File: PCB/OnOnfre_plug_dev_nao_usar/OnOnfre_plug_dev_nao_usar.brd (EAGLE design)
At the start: 44.4 x 47.7 mm, 41 parts, among them IC4 HLW8012, J7 8p, Q3 2N7002, Q4 2N7002, U2 esp12

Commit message: Labels Fix
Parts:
- removed R5: VARISTORS07K230, varistor:S07K230
- moved R31 113.5 mm to (22.1, 38.4), turned to 180 degrees
- moved R45 111.2 mm to (25.4, 38.4)
- moved R47 110.2 mm to (28.4, 37.8), turned to 270 degrees
- moved R48 110.1 mm to (31.0, 37.8), turned to 90 degrees
- moved R32 109.5 mm to (30.5, 33.0), turned to 180 degrees
- moved R46 108.5 mm to (25.4, 36.1), turned to 180 degrees
- moved R49 100.5 mm to (42.7, 27.2), turned to 180 degrees
- moved R55 98.4 mm to (17.3, 21.3), turned to 180 degrees
- moved R54 97.2 mm to (17.3, 19.6), turned to 180 degrees
- moved R53 96.3 mm to (17.3, 17.8), turned to 180 degrees
- moved R50 96.0 mm to (17.3, 23.4)
- moved R52 90.1 mm to (17.3, 16.0), turned to 180 degrees
- moved C44 89.8 mm to (6.10, 22.4), turned to 270 degrees
- moved C42 89.5 mm to (3.05, 22.4), turned to 270 degrees
- moved R43 88.4 mm to (5.84, 16.5)
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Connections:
- net LINE_IN: now also U$2.P$2; no longer R5.1, U$2.P$1
- net NEUTRAL_IN: now also U$2.P$1; no longer R5.2, U$2.P$2
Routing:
- net 5V: track 45.7 -> 0.00 mm, vias 1 -> 0
- net NEUTRAL_IN: track 50.8 -> 17.2 mm
- net GND: track 81.8 -> 63.9 mm, vias 3 -> 0
- net GPIO04: track 13.9 -> 0.00 mm
- net NC: track 9.81 -> 0.00 mm
- net LINE_IN: track 7.28 -> 13.4 mm
- net NO: track 4.80 -> 0.00 mm
- net GPIO05: track 6.68 -> 3.64 mm
- net N$6: track 0.00 -> 2.26 mm
- net V2P: track 0.00 -> 2.03 mm
- net N$8: track 0.00 -> 1.78 mm
- net N$16: track 0.00 -> 1.78 mm
- net N$15: track 0.00 -> 1.78 mm
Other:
- board size 44.4 x 47.7 mm -> 44.8 x 47.8 mm
- board text removed: "230V"
- board text removed: "2A MAX"
- board text removed: "2ADSS"
- board text removed: "BH-OnOfre"
- board text removed: "DANGER HIGH VOLTAGE"
- board text removed: "rev3.4"

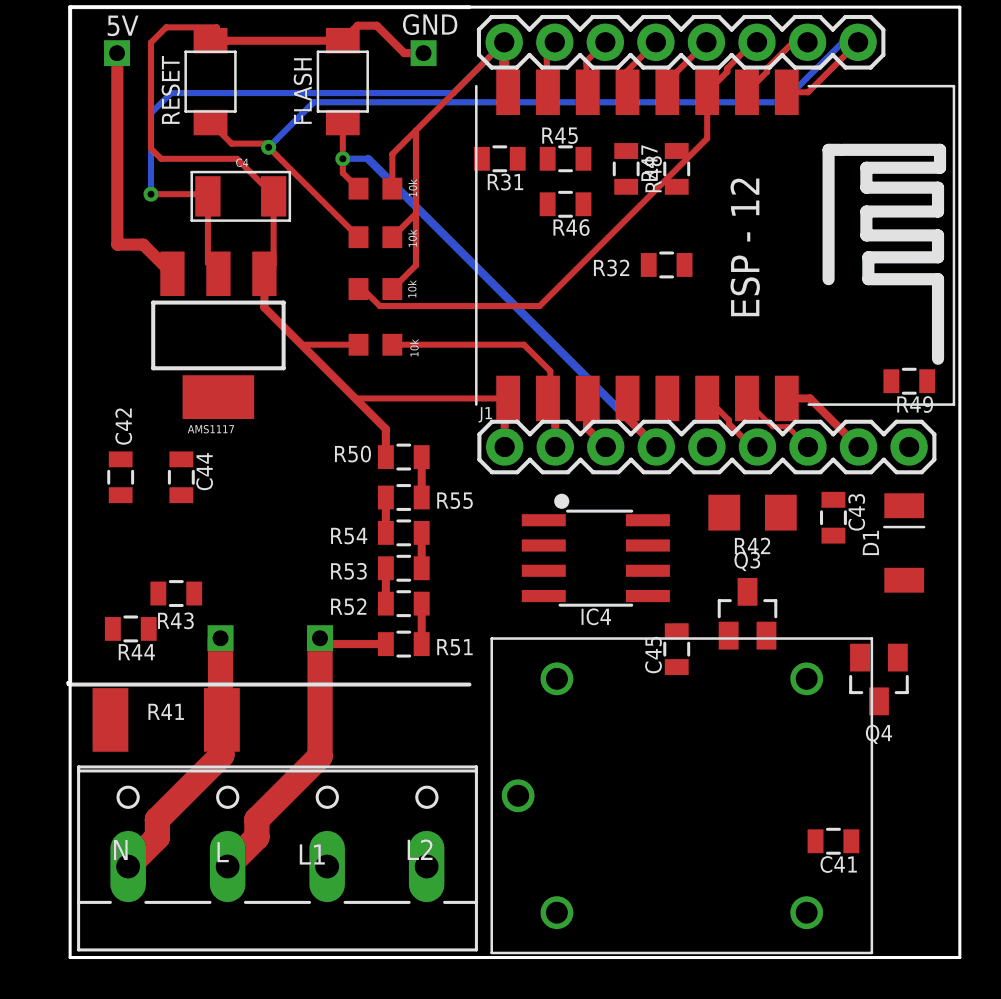
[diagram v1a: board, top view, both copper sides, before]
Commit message: remoção do OTA Arduino e adição de OTA via Web
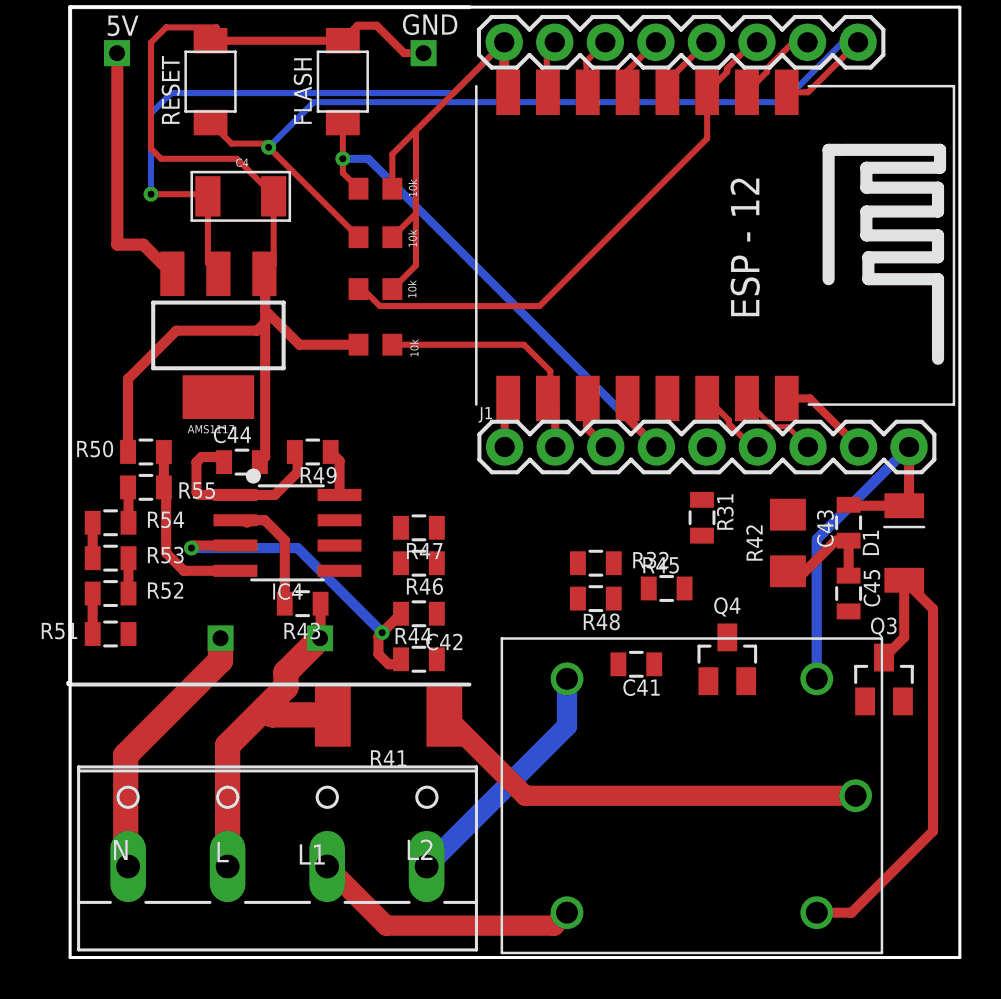
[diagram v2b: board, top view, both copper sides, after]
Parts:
- moved R49 30.2 mm to (12.7, 23.6)
- moved R45 22.2 mm to (30.5, 16.8)
- moved R48 22.0 mm to (26.9, 16.3), turned to 180 degrees
- moved R47 20.8 mm to (18.0, 19.8), turned to 180 degrees
- moved R31 20.7 mm to (32.3, 20.3), turned to 270 degrees
- moved R46 19.5 mm to (18.0, 18.0)
- moved C42 16.5 mm to (18.0, 15.5), turned to 180 degrees
- moved IC4 15.5 mm to (9.65, 21.8)
- moved R32 15.4 mm to (26.9, 18.0), turned to 0 degrees
- moved R51 14.7 mm to (2.54, 14.5), turned to 0 degrees
- moved R52 14.7 mm to (2.54, 16.5), turned to 0 degrees
- moved R53 14.7 mm to (2.54, 18.3), turned to 0 degrees
- moved R54 14.7 mm to (2.54, 20.1), turned to 0 degrees
- moved R44 14.6 mm to (18.0, 13.2), turned to 0 degrees
- moved C41 13.3 mm to (29.0, 13.0)
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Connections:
- net LINE_IN: now also U$2.P$1, X1.2; no longer U$2.P$2, X1.1
- net NC: now also X1.3; no longer X1.4
- net NEUTRAL_IN: now also U$2.P$2, X1.1; no longer U$2.P$1, X1.2
- net NO: now also X1.4; no longer X1.3
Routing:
- net 5V: track 0.00 -> 29.2 mm
- net N$4: track 0.00 -> 25.1 mm
- net LINE_R: track 0.00 -> 22.3 mm
- net N$14: track 0.00 -> 17.6 mm, vias 0 -> 2
- net NC: track 0.00 -> 13.6 mm
- net NO: track 0.00 -> 12.4 mm
- net V2P: track 2.03 -> 8.98 mm
- net N$12: track 0.00 -> 6.72 mm
- net LINE_IN: track 13.4 -> 18.7 mm
- net GND: track 63.9 -> 67.7 mm
- net NEUTRAL_IN: track 17.2 -> 13.5 mm
- net N$10: track 0.00 -> 2.34 mm
- net N$3: track 0.00 -> 0.51 mm
